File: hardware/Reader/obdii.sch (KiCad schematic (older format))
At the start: 1 part

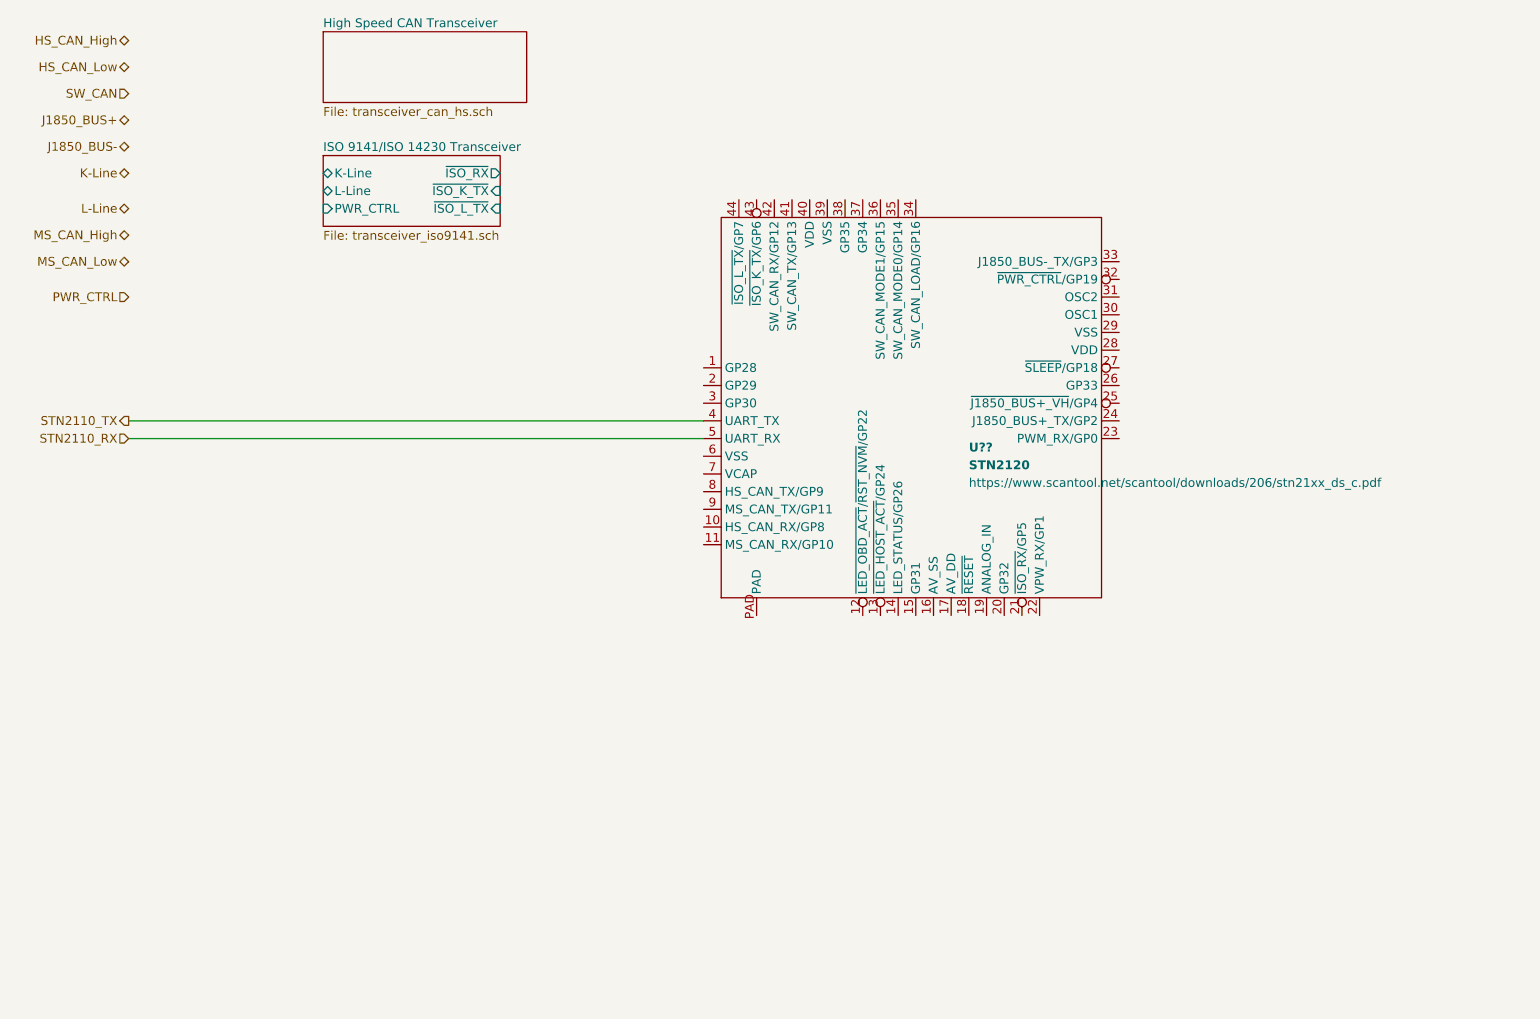
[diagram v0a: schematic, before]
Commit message: Completed schematics for reader
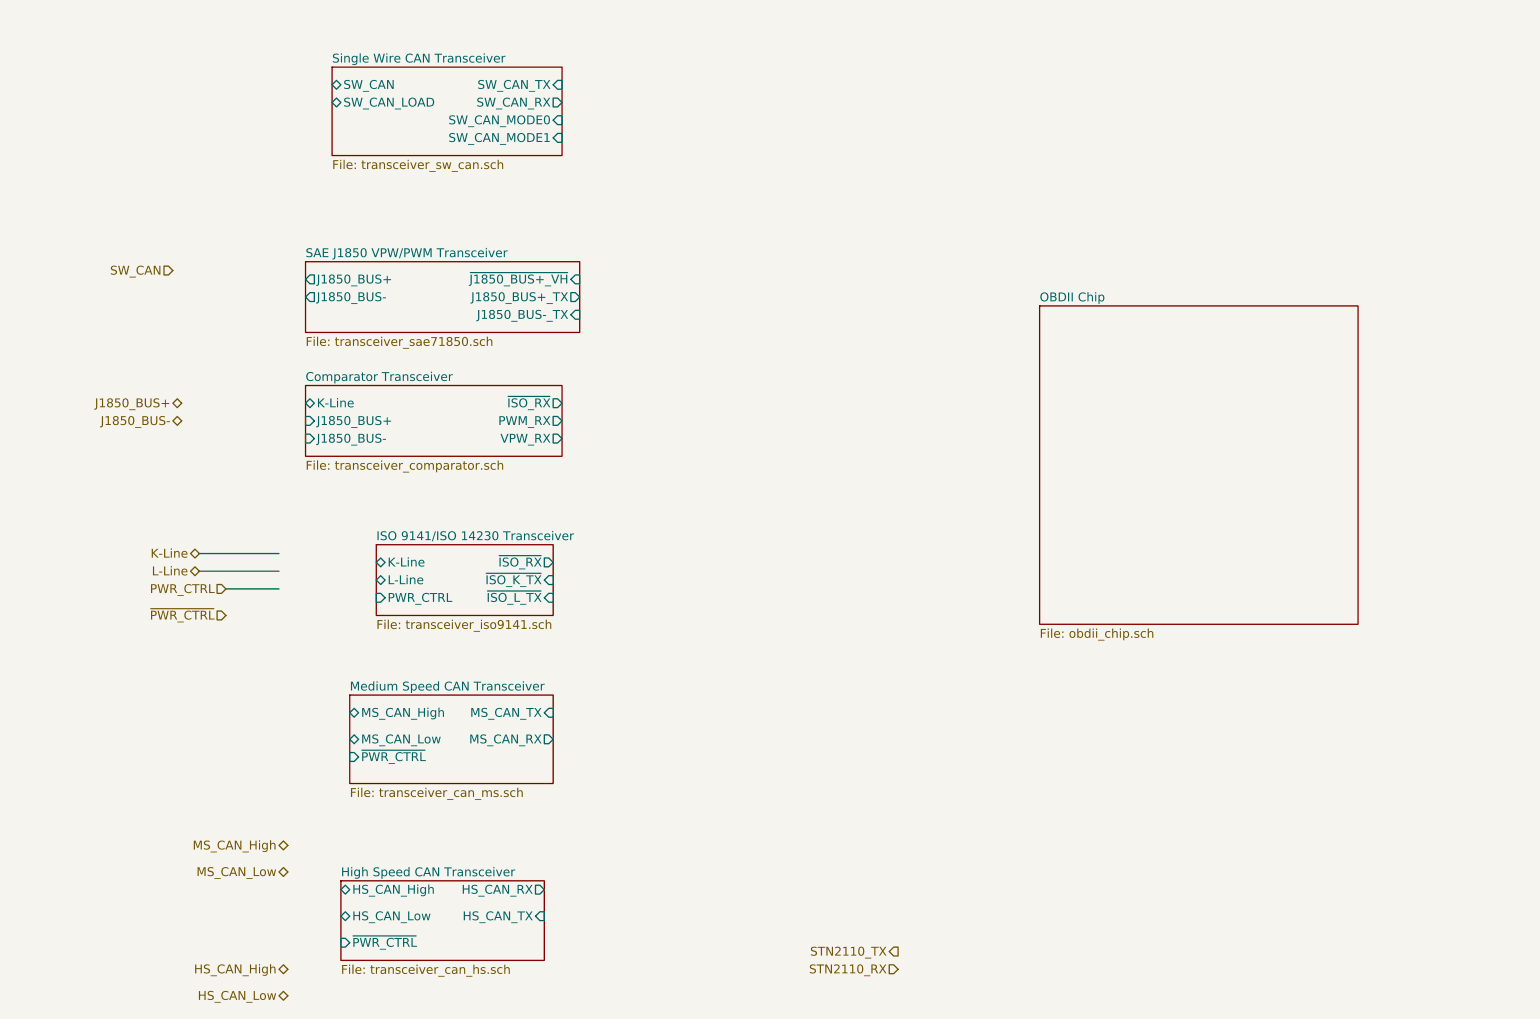
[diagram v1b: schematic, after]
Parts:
- removed U??: STN2120, symbol CANtech:STN2120
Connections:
- net labels added: ~PWR_CTRL~
- wire segments 2 -> 3
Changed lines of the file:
@@
 $Descr USLetter 11000 8500
 encoding utf-8
-Sheet 5 9
+Sheet 5 14
 Title ""
 Date "2020-10-18"
@@
 Comment4 ""
 $EndDescr
-Text HLabel 1250 1550 0    50   BiDi ~ 0
+Text HLabel 1650 3700 0    50   BiDi ~ 0
 K-Line
-Text HLabel 1250 1750 0    50   BiDi ~ 0
+Text HLabel 1650 3800 0    50   BiDi ~ 0
 L-Line
-Text HLabel 1250 800  0    50   BiDi ~ 0
+Text HLabel 2150 6050 0    50   BiDi ~ 0
 HS_CAN_High
-Text HLabel 1250 950  0    50   BiDi ~ 0
+Text HLabel 2150 6200 0    50   BiDi ~ 0
 HS_CAN_Low
-Text HLabel 1250 1100 0    50   Input ~ 0
+Text HLabel 1500 2100 0    50   Input ~ 0
 SW_CAN
-Text HLabel 1250 1250 0    50   BiDi ~ 0
+Text HLabel 1550 2850 0    50   BiDi ~ 0
 J1850_BUS+
-Text HLabel 1250 1400 0    50   BiDi ~ 0
+Text HLabel 1550 2950 0    50   BiDi ~ 0
 J1850_BUS-
-Text HLabel 1250 1900 0    50   BiDi ~ 0
+Text HLabel 2150 5350 0    50   BiDi ~ 0
 MS_CAN_High
-Text HLabel 1250 2050 0    50   BiDi ~ 0
+Text HLabel 2150 5500 0    50   BiDi ~ 0
 MS_CAN_Low
-Text HLabel 1250 2950 0    50   Output ~ 0
+Text HLabel 5600 5950 0    50   Output ~ 0
 STN2110_TX
-$Comp
-L CANtech:STN2120 U??
-U 1 1 5FA4C6F8
-P 5800 2800
-F 0 "U??" H 6000 2500 50  0000 L CNB
-F 1 "STN2120" H 6000 2400 50  0000 L CNB
-F 2 "" H 6100 2450 50  0000 C CNN
-F 3 "https://www.scantool.net/scantool/downloads/206/stn21xx_ds_c.pdf" H 6000 2300 50  0000 L CNN
-	1    5800 2800
-	1    0    0    -1
-$EndComp
-Text HLabel 1250 2250 0    50   Input ~ 0
+Text HLabel 1800 3900 0    50   Input ~ 0
 PWR_CTRL
 $Sheet
-S 2350 1450 1000 400
+S 2650 3650 1000 400
 U 5FA83833
 F0 "ISO 9141/ISO 14230 Transceiver" 50
 F1 "transceiver_iso9141.sch" 50
-F2 "~ISO_RX~" O R 3350 1550 50
-F3 "~ISO_K_TX~" I R 3350 1650 50
-F4 "PWR_CTRL" I L 2350 1750 50
-F5 "~ISO_L_TX~" I R 3350 1750 50
-F6 "K-Line" B L 2350 1550 50
-F7 "L-Line" B L 2350 1650 50
+F2 "~ISO_RX~" O R 3650 3750 50
+F3 "~ISO_K_TX~" I R 3650 3850 50
+F4 "PWR_CTRL" I L 2650 3950 50
+F5 "~ISO_L_TX~" I R 3650 3950 50
+F6 "K-Line" B L 2650 3750 50
+F7 "L-Line" B L 2650 3850 50
 $EndSheet
 $Sheet
-S 2350 750  1150 400
+S 2450 5550 1150 450
 U 5FAEE035
 F0 "High Speed CAN Transceiver" 50
 F1 "transceiver_can_hs.sch" 50
+F2 "HS_CAN_High" B L 2450 5600 50
+F3 "HS_CAN_Low" B L 2450 5750 50
+F4 "~PWR_CTRL~" I L 2450 5900 50
+F5 "HS_CAN_TX" I R 3600 5750 50
+F6 "HS_CAN_RX" O R 3600 5600 50
 $EndSheet
-Text HLabel 1250 3050 0    50   Input ~ 0
+Text HLabel 5600 6050 0    50   Input ~ 0
 STN2110_RX
+Text HLabel 1800 4050 0    50   Input ~ 0
+~PWR_CTRL~
 Wire Wire Line
-	1250 3050 4500 3050
+	1800 3900 2100 3900
 Wire Wire Line
-	1250 2950 4500 2950
+	1650 3700 2100 3700
+Wire Wire Line
+	1650 3800 2100 3800
+$Sheet
+S 2500 4500 1150 500
+U 5FB34A7C
+F0 "Medium Speed CAN Transceiver" 50
+F1 "transceiver_can_ms.sch" 50
+F2 "MS_CAN_High" B L 2500 4600 50
+F3 "MS_CAN_Low" B L 2500 4750 50
+F4 "~PWR_CTRL~" I L 2500 4850 50
+F5 "MS_CAN_TX" I R 3650 4600 50
+F6 "MS_CAN_RX" O R 3650 4750 50
+$EndSheet
+$Sheet
+S 2250 2050 1550 400
+U 5FB3FEAD
+F0 "SAE J1850 VPW/PWM Transceiver" 50
+F1 "transceiver_sae71850.sch" 50
+F2 "~J1850_BUS+_VH~" I R 3800 2150 50
+F3 "J1850_BUS+_TX" O R 3800 2250 50
+F4 "J1850_BUS+" O L 2250 2150 50
+F5 "J1850_BUS-_TX" I R 3800 2350 50
+F6 "J1850_BUS-" O L 2250 2250 50
+$EndSheet
+$Sheet
+S 2250 2750 1450 400
+U 5FB4CA84
+F0 "Comparator Transceiver" 50
+F1 "transceiver_comparator.sch" 50
+F2 "~ISO_RX~" O R 3700 2850 50
+F3 "K-Line" B L 2250 2850 50
+F4 "J1850_BUS+" I L 2250 2950 50
+F5 "J1850_BUS-" I L 2250 3050 50
+F6 "PWM_RX" O R 3700 2950 50
+F7 "VPW_RX" O R 3700 3050 50
+$EndSheet
+$Sheet
+S 2400 950  1300 500
+U 5FBCBEA5
+F0 "Single Wire CAN Transceiver" 50
+F1 "transceiver_sw_can.sch" 50
+F2 "SW_CAN" B L 2400 1050 50
+F3 "SW_CAN_TX" I R 3700 1050 50
+F4 "SW_CAN_RX" O R 3700 1150 50
+F5 "SW_CAN_MODE0" I R 3700 1250 50
+F6 "SW_CAN_MODE1" I R 3700 1350 50
+F7 "SW_CAN_LOAD" B L 2400 1150 50
+$EndSheet
+$Sheet
+S 6400 2300 1800 1800
+U 5FC0631B
+F0 "OBDII Chip" 50
+F1 "obdii_chip.sch" 50
+$EndSheet
 $EndSCHEMATC
